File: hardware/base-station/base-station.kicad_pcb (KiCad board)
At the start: 4 copper layers, 30.3 x 90.5 mm, 114 parts, among them J2 USB4110GFA, J4 S3B-XH-A, J6 Conn_01x04, Q1 FS8205A, Q2 FS8205A, Q3 FS8205A, U1 W25Q128JVSIQ, U12 MP2672AGD-0000-Z, U14 DW01A, U15 479480001, U2 TPS61023DRLR, U22 TPS22918DBVR, U3 ESP32-S3RH2, U5 BQ21040DBVR, U9 TPS63020DSJR, Y1 SC-32S-32.768kHz-12.5pF, Y2 ECS-400-10-37B2-CKY-TR

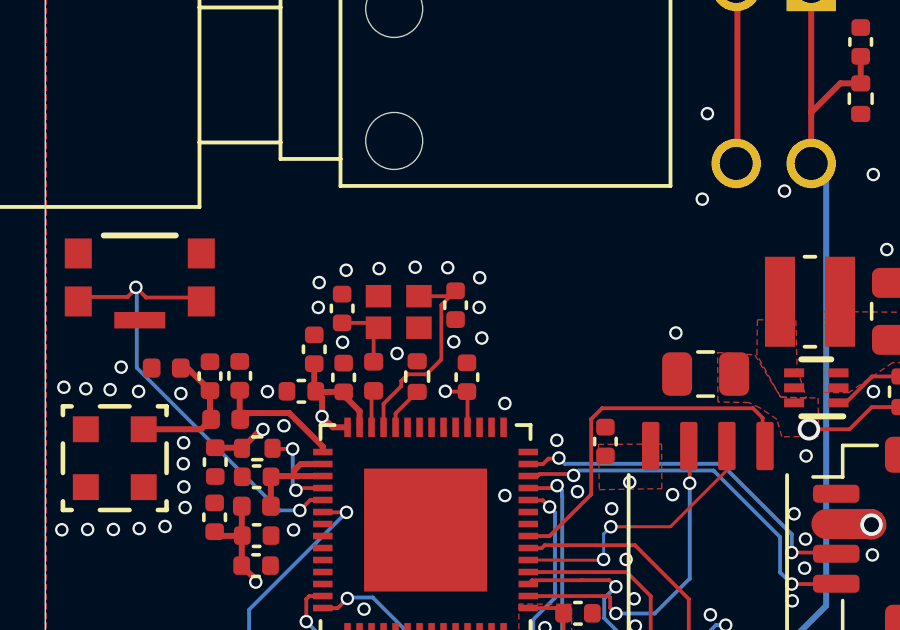
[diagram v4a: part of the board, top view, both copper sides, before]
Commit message: hardware: drop the 24 nH series inductor from all three S3 crystal legs
Every ESP32-S3 board put a 24 nH in series with XTAL_P -- base L2, rocket L3,
LoRa L10 -- inherited from a reference design. The P4's crystal never had one.
Measured against what it actually does at 40 MHz, it does not earn the part:

  reactance         6.0 ohm, against 331 ohm for the 12 pF load cap
  frequency effect  -1.1 ppm (it makes the leg's cap look 1.8% larger)
  low-pass corner   297 MHz with the load cap -- trims the 8th harmonic up,
                    which was its only defensible function
  resonance w/ C0   726 MHz, where the oscillator has no gain, so it was
                    never a risk either

Removing it leaves each XTAL_P as a direct U.54 - Y.3 - C.1 connection and
takes one 0402 plus one BOM line out of all three boards. The RF matching
networks are untouched: rocket keeps L1 4.3 nH / L2 2.7 nH / L4 2 nH, base
keeps L4 4.3 nH / L7 2.7 nH / L3 2 nH, LoRa keeps L11 2 nH (supply filter --
that board has no antenna and LNA_IN is deliberately unconnected).

Frequency error at 12 pF after the change:

  lora   Y6 -> U28   11.97 mm avg   +8.6 ppm
  rocket Y2 -> U15   11.54 mm avg   +9.2 ppm
  rocket Y4 -> U17   11.97 mm avg   +8.6 ppm
  base   Y2 -> U3     7.58 mm avg  +15.1 ppm   <- #704 still open

Cross-board BOM: the 24 nH line (LQW15AN24NH00D) is retired, quantities
cleared rather than the row deleted, per the sheet's existing convention.
System cost 122.58 -> 122.28 per set. All four costed boards still reconcile
exactly: 424 fitted parts, 0 quantity mismatches, 0 parts without a BOM row.

Refs #704

Co-Authored-By: Claude Opus 5 <noreply@anthropic.com>
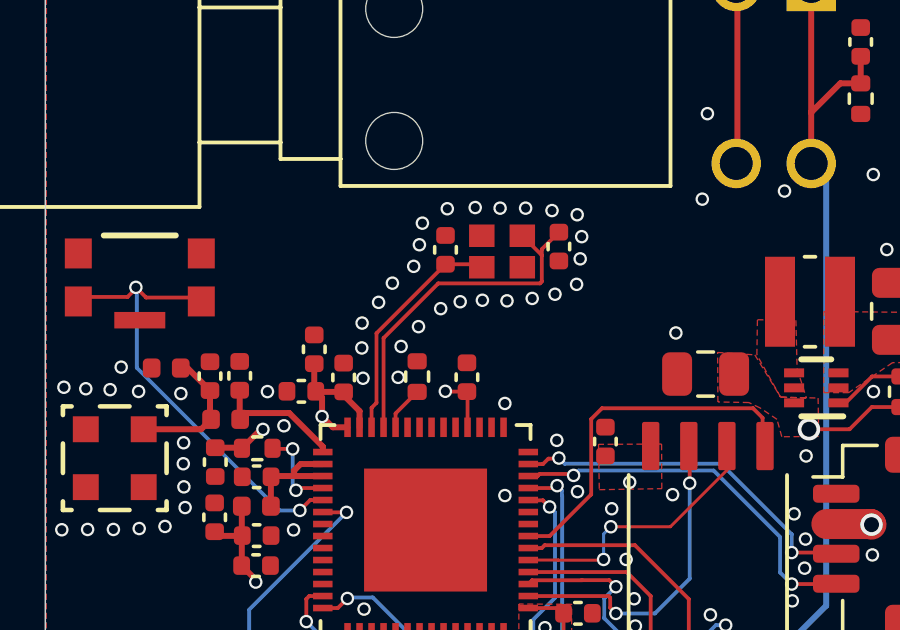
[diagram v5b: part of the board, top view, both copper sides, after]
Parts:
- removed L2: 24 nH, Inductor_SMD:L_0402_1005Metric
- C3, C6: value 18 pF -> 12 pF
- Y1: value SC-32S-32.768kHz-12.5pF -> ABS07-32.768KHZ-T
- moved Y2 3.99 mm to (62.6, 142.5)
- moved C3 3.96 mm to (60.7, 142.5)
- moved C6 3.96 mm to (64.5, 142.4)
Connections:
- C23 pad 1: Net-(U22-QOD) -> V_SWITCH
- C3 pad 1: Net-(C3-Pad1) -> Net-(U3-XTAL_P)
- C34 pad 1: VCC -> V_SWITCH
- C59 pad 1: Net-(U22-QOD) -> V_SWITCH
- C8 pad 1: +3V3 -> Net-(U3-CHIP_PU)
- L8 pad 1: VCC -> V_SWITCH
- R1 pad 1: Net-(U3-CHIP_PU) -> +3V3
- R1 pad 2: +3V3 -> Net-(U3-CHIP_PU)
- U2 pad 2: VCC -> V_SWITCH
- U2 pad 3: VCC -> V_SWITCH
- U22 pad 5: Net-(U22-QOD) -> V_SWITCH
- U22 pad 6: Net-(U22-QOD) -> V_SWITCH
- U9 pad 10: Net-(U22-QOD) -> V_SWITCH
- U9 pad 11: Net-(U22-QOD) -> V_SWITCH
- Y2 pad 3: Net-(C3-Pad1) -> Net-(U3-XTAL_P)
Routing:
- net Net-(U3-XTAL_P): track 1.24 -> 7.71 mm
- net Net-(U3-XTAL_N): track 7.20 -> 11.8 mm
- net Net-(C3-Pad1): track 2.48 -> 0.00 mm
- net Net-(U3-CHIP_PU): track 3.03 -> 4.89 mm
- net +3V3: track 18.9 -> 17.1 mm
- net GND: track 2.69 -> 2.70 mm, vias 124 -> 138
- added copper zone on F.Cu, net V_SWITCH
- removed copper zone on F.Cu, net Net-(U22-QOD)

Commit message: hardware(base-station): lengthen the 40 MHz clock legs to match the other boards
#704: the base station's crystal traces were less than half the length of the
other three networks, so the 12 pF load caps that suit every other board left
this one under-loaded and running fast. Y2 moved further from U3 and both legs
re-routed; XTAL_P 6.76 -> 8.94 mm, XTAL_N 8.41 -> 11.83 mm, average 7.58 ->
10.38 mm.

All four networks are now matched to within 2.3 ppm:

  lora   Y6 -> U28   11.97 mm avg   +8.6 ppm
  rocket Y2 -> U15   11.54 mm avg   +9.2 ppm
  rocket Y4 -> U17   11.97 mm avg   +8.6 ppm
  base   Y2 -> U3    10.38 mm avg  +10.9 ppm

Every clock net is on a single layer with zero vias, per Espressif's rule.

Stopping at +10.9 rather than chasing the last 0.9 ppm of copper is deliberate.
The absolute figure assumes C_m = 5 fF and C_0 = 2 pF -- typical for a 3225
AT-cut but NOT read off the ECS datasheet -- and sweeping those across
plausible values puts this network anywhere from +8.1 to +15.4 ppm, so 0.9 ppm
is well inside the model's own uncertainty. What the model does resolve
reliably is the difference between boards, since that depends only on delta
C_L, and by that measure the four are now equivalent.

DEFERRED, unchanged from the issue: measure the 40 MHz output on the first
article and trim if needed. The trim needs no layout work -- C3/C6 at 13 pF
moves this network to +1.8 ppm in the same footprint.

Refs #704

Co-Authored-By: Claude Opus 5 <noreply@anthropic.com>
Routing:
- net Net-(U3-XTAL_P): track 7.71 -> 8.94 mm
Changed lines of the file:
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@@
 	)
 	(via
-		(at 58.51 144.23)
+		(at 57.97 143.92)
 		(size 0.45)
 		(drill 0.3)
@@
 	)
 	(via
-		(at 59.68 143.03)
+		(at 58.49 142.52)
 		(size 0.45)
 		(drill 0.3)
@@
 	)
 	(via
-		(at 60.58 144.44)
+		(at 60.46 144.57)
 		(size 0.45)
 		(drill 0.3)
@@
 	)
 	(via
-		(at 59.87 142.31)
+		(at 59.29 142.14)
 		(size 0.45)
 		(drill 0.3)
@@
 	)
 	(via
-		(at 58.97 143.59)
+		(at 58.04 143.2)
 		(size 0.45)
 		(drill 0.3)
@@
 	)
 	(segment
-		(start 58.44 145.26)
-		(end 60.74 142.96)
+		(start 61.85 142.96)
+		(end 61.95 143.06)
 		(width 0.127)
 		(layer "F.Cu")
@@
 	)
 	(segment
-		(start 61.85 142.96)
-		(end 61.95 143.06)
+		(start 58.44 143.16)
+		(end 58.64 142.96)
 		(width 0.127)
 		(layer "F.Cu")
@@
 	)
 	(segment
-		(start 58.275 148.395)
-		(end 58.275 147.745)
+		(start 58.275 147.745)
+		(end 58.44 147.58)
 		(width 0.127)
 		(layer "F.Cu")
@@
 	)
 	(segment
-		(start 58.44 147.58)
-		(end 58.44 145.26)
+		(start 60.74 142.96)
+		(end 61.85 142.96)
 		(width 0.127)
 		(layer "F.Cu")
@@
 	)
 	(segment
-		(start 60.74 142.96)
-		(end 61.85 142.96)
+		(start 58.64 142.96)
+		(end 60.74 142.96)
 		(width 0.127)
 		(layer "F.Cu")
@@
 	)
 	(segment
-		(start 58.275 147.745)
-		(end 58.44 147.58)
+		(start 58.44 147.58)
+		(end 58.44 143.16)
+		(width 0.127)
+		(layer "F.Cu")
+		(net "Net-(U3-XTAL_P)")
+	)
+	(segment
+		(start 58.275 148.395)
+		(end 58.275 147.745)
 		(width 0.127)
 		(layer "F.Cu")

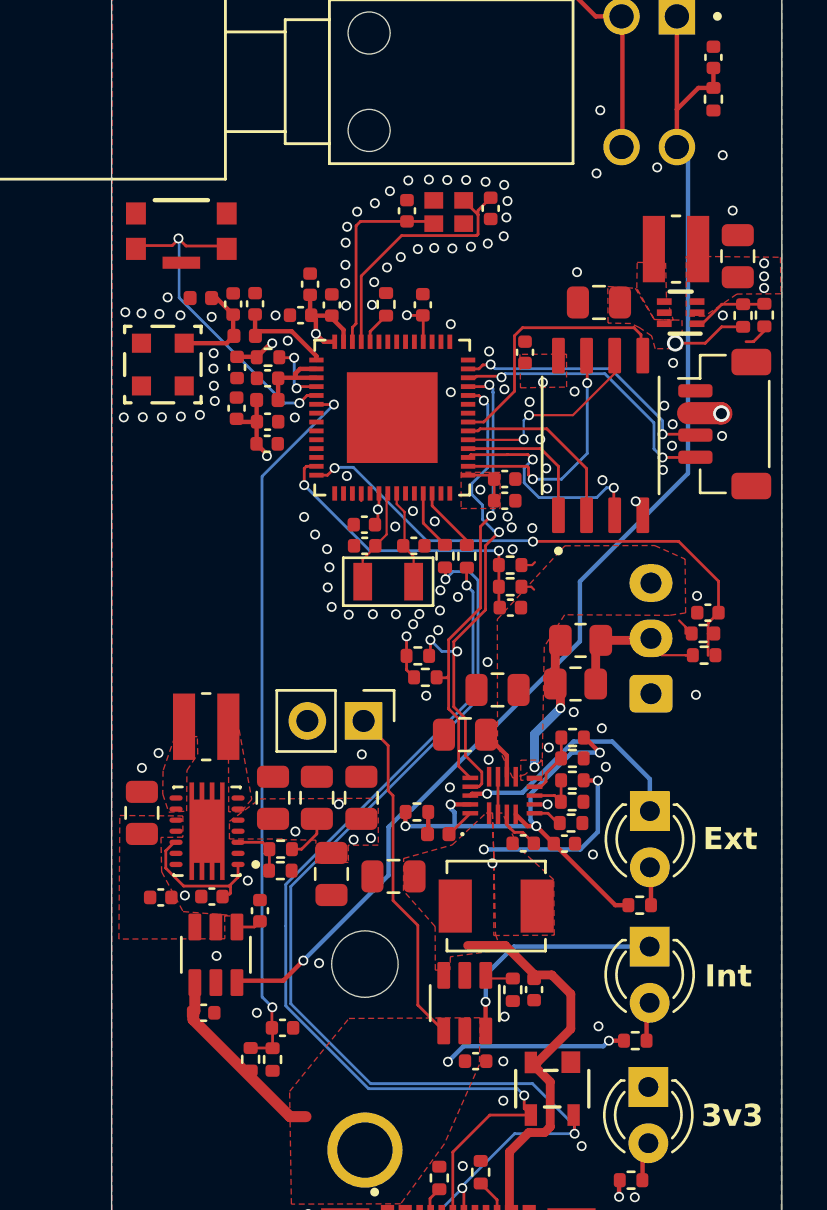
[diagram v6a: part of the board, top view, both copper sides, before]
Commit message: hardware(base-station): pre-fab fixes -- JLC stackup, RF feed, R17/R18, EN margin
The board changes the 2026-08-02 pre-manufacturing review called for. Board is
DRC-clean: 0 errors, 0 unconnected items, 0 schematic-parity issues.

Electrical:
- R17 10 k -> 18.7 k and R18 1 k, both with MPNs that match their values. Both
  previously carried RC0402FR-075K11L (5.11 k). Built to that MPN the TPS61023
  EN pin would sit at 1.65 V driven low, above the 1.2 V V_EN_H ceiling, and the
  LoRa power-cycle recovery would never work with no symptom. 18.7 k/1 k gives
  0.174 V against the 0.35 V guaranteed-low floor, and is already a fleet MPN so
  it adds no BOM line.
- Antenna matching reduced to Molex section 6.0: L4 4.3 nH shunt alone, with
  C2 = 0 ohm realised as a direct trace. C25/C26/L7 removed. The previous
  four-element network put 4.3 nH in parallel with 1.5 pF, which is -j127.8 ohm
  at 2.44 GHz where the Molex reference is +j65.9 ohm -- a sign inversion, not a
  value shift. Accepted trade: this build has no tuning provision, so it must be
  characterised with the cell installed and the result carried into the next
  revision.
- U15 fixing pads 1-3 left individually unconnected. AS-479480001 calls them
  fixing pads and never specifies their net; grounding them is an unforced risk
  on an LDS part whose plating wraps the body.

Stackup and rules, now JLCPCB standard 4-layer:
- JLC04161H-7628: 0.2104 mm 7628 prepreg (Er 4.4), 0.5 oz inner copper, 1.065 mm
  core, ENIG, 1.5862 mm. The previous 0.1 mm prepreg and 1 oz inner layers were
  not a stackup any standard 4-layer order builds.
- RF feed re-solved for the new dielectric: 0.20 -> 0.36 mm, giving 49.7 ohm as
  CPWG at the 0.15 mm pour gap. At 0.20 mm on the new stackup it would have been
  ~68 ohm. New RF netclass carries the width and clearance.
- min_clearance 0.09 -> 0.10 (0.09 falls in the JLC 3.0-3.5 mil upcharge band),
  min_via_diameter 0.40 -> 0.45, annular 0.05 -> 0.075, drill 0.1 -> 0.3, silk
  text 0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
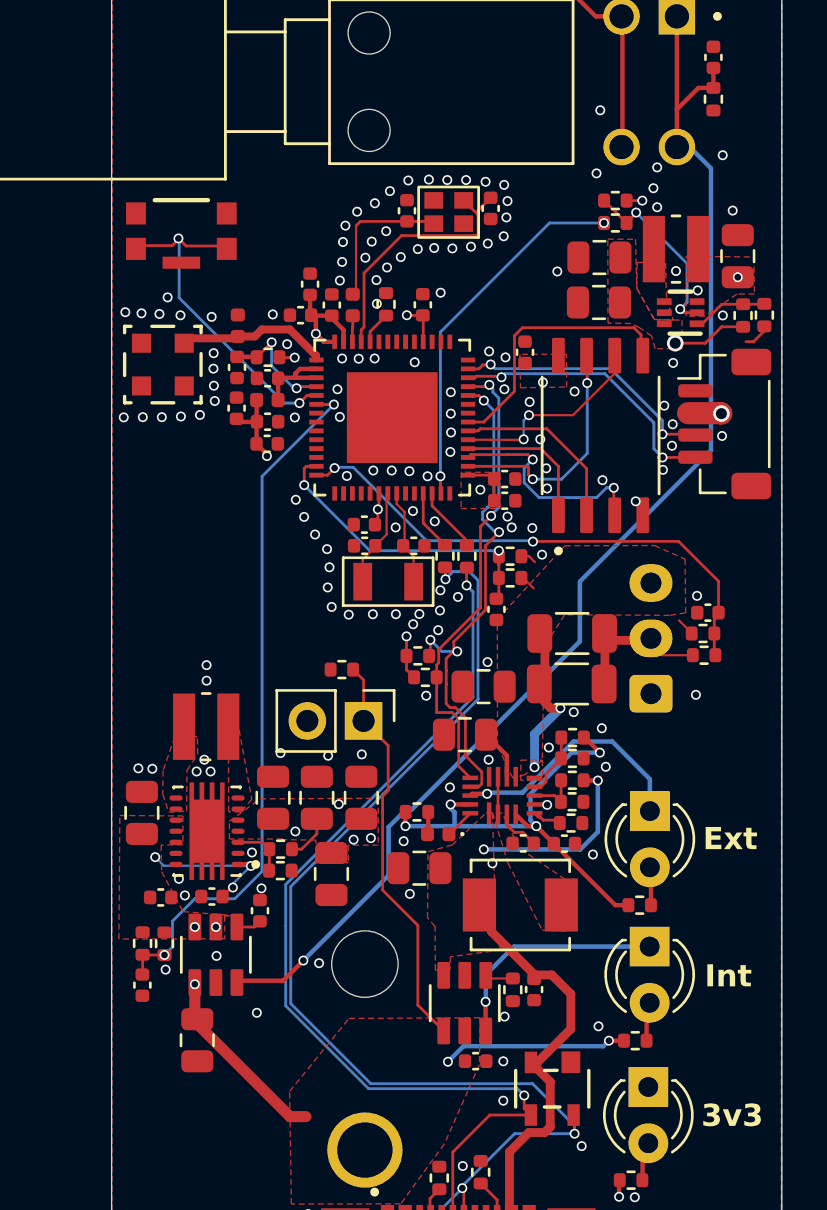
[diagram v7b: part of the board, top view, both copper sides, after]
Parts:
- removed C25, C26: 1.5 pF, Capacitor_SMD:C_0402_1005Metric
- removed L7: 2.7 nH, Inductor_SMD:L_0402_1005Metric
- added C41: 22 uF, Capacitor_SMD:C_0805_2012Metric, F.Cu at (69.4, 144.6)
- added L2: 24 nH, Inductor_SMD:L_0402_1005Metric, F.Cu at (58.3, 146.7)
- added R17: 18.7 k, Resistor_SMD:R_0402_1005Metric, F.Cu at (70.2, 142.0)
- added R18: 1 k, Resistor_SMD:R_0402_1005Metric, F.Cu at (70.2, 143.0)
- added R53: 210 k, Resistor_SMD:R_0402_1005Metric, F.Cu at (57.8, 163.2)
- C42: value 1 uF -> 22 uF; footprint Capacitor_SMD:C_0402_1005Metric -> Capacitor_SMD:C_0805_2012Metric
- R43: value 6.04 k -> 10 k
- R45, R47: footprint Resistor_SMD:R_0805_2012Metric -> Resistor_SMD:R_1206_3216Metric
- moved R46 7.87 mm to (48.8, 175.6), turned to 90 degrees
- moved C30 6.62 mm to (48.8, 177.4), turned to -90 degrees
- moved R44 6.51 mm to (49.8, 175.6), turned to -90 degrees
- moved L4 2.09 mm to (53.1, 147.7), turned to -90 degrees
- moved C42 1.27 mm to (51.3, 179.9), turned to -90 degrees
- moved C48 1.23 mm to (61.3, 172.2)
- moved L6 1.09 mm to (65.9, 173.8)
- moved C54 0.65 mm to (64.2, 164.0)
- moved C55 0.64 mm to (64.8, 160.5), turned to 90 degrees
- moved R47 0.49 mm to (68.2, 161.6)
- moved R40 0.40 mm to (65.4, 159.1)
- moved R42 0.40 mm to (65.4, 158.1)
- moved R45 0.17 mm to (68.2, 163.8)
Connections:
- C29 pad 1: Net-(U9-EN) -> V_SWITCH
- C3 pad 1: Net-(U3-XTAL_P) -> Net-(C3-Pad1)
- R44 pad 1: VCC -> V_SWITCH
- U2 pad 2: V_SWITCH -> Net-(U2-EN)
- U3 pad 1: Net-(U3-LNA_IN) -> Net-(U15-Feed)
- U3 pad 10: M_MOSI -> unconnected-(U3-GPIO5-Pad10)
- U3 pad 11: M_FLASH_CS -> unconnected-(U3-GPIO6-Pad11)
- U3 pad 12: M_MISO -> unconnected-(U3-GPIO7-Pad12)
- U3 pad 27: unconnected-(U3-GPIO21-Pad27) -> LoRa_EN
- U3 pad 9: M_SCK -> unconnected-(U3-GPIO4-Pad9)
- U9 pad 1: Net-(U9-EN) -> V_SWITCH
- U9 pad 12: Net-(U9-EN) -> V_SWITCH
- Y2 pad 3: Net-(U3-XTAL_P) -> Net-(C3-Pad1)
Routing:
- net V_SWITCH: track 0.00 -> 54.2 mm, vias 0 -> 7
- net LoRa_EN: track 0.00 -> 16.7 mm, vias 0 -> 2
- net VCC: track 112.5 -> 99.3 mm, vias 5 -> 3
- net Net-(U2-EN): track 0.00 -> 8.35 mm, vias 0 -> 2
- net Net-(U3-XTAL_P): track 8.94 -> 1.18 mm
- net Net-(C3-Pad1): track 0.00 -> 6.79 mm
- net Net-(U9-EN): track 6.55 -> 0.00 mm
- net Net-(U3-LNA_IN): track 4.46 -> 0.00 mm
- net Net-(U5-TS): track 15.5 -> 18.2 mm
- net Net-(U15-Feed): track 4.64 -> 6.83 mm
- net +3V3: track 17.1 -> 18.6 mm, vias 11 -> 12
- net Net-(U22-ON): track 57.1 -> 58.0 mm
- net Net-(U12-MID): track 6.41 -> 7.08 mm
- net Volt_Read: track 32.4 -> 31.8 mm
- net VBUS: track 33.2 -> 33.8 mm
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
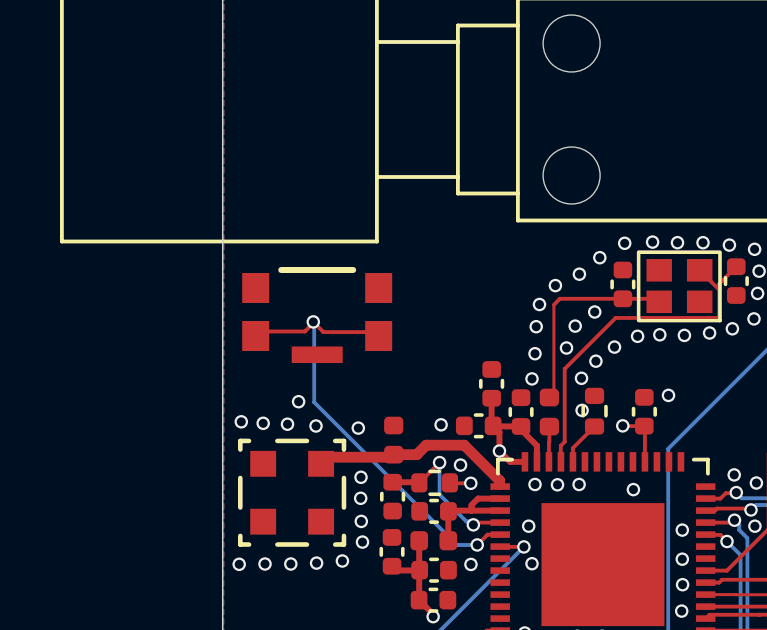
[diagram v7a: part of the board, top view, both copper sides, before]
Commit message: hardware(rocket-computer): V9 pre-fab review close-out -- every finding fixed, measured, or waived
Closes the 2026-08-04..09 pre-manufacturing review (170 raw findings).
WORKLIST.md is the closing record: D-1..D-4 decided, H-1..H-10 and
M-1..M-25 dispositioned, Lows annotated, bench list is the remainder.

Power architecture:
- All four peripheral branches converted low-side N-FET -> integrated
  high-side switches (U26/U28 TPS22811LRPWR, U27/U29 TPS22810DRVR);
  U30 TPS22810DRVR gates the P4 domain. Every connector ground is now
  hard GND; the 12 EXP lines stay resistor-free by design (H-3/D-4).
  J3 and J4 power pins swapped ends -- fab notes B6/B7 carry the
  harness warnings.
- Q11 (CSD25404Q3) reverse-polarity P-FET at the battery input on a
  new TI-pattern footprint; CR2 re-purposed as connector ESD clamp
  upstream of it (M-9/M-10). Kelvin sense at R72 preserved.
- P4 rail self-latch: D9 (BAV170M) OR-gates S3 request with P4 hold,
  C105 rides the P4 through its own reset (H-4; firmware in #718).
- eFuse UVLO deglitch C94 (H-1); brownout decided as clean-reboot,
  ECO hold-up claims corrected in power-eco.md (H-8/D-3).
- Pyro gate-drive stiffened: R22 -> 5.11k, R78-R81 shunts (H-2).
- Servo budget decided at 3 A set by the In2 stretch; ILIM left open
  at 11.6 A; SERVO_IMON flight data gates any increase (D-1).

Component and BOM:
- TPS2121 ILIM 18.7k -> 49.9k (real protection at 2.26 A typ, M-5).
- IMON scaling: R85 -> 2.2k (3 A camera), R88 -> 1k (servo open).
- C27 VDD_SPI 10u -> 1u per HDG (M-4); switch VIN bypass 100n -> 1u;
  C40/C76 consolidation; C65 MPN fixed (was a 390 pF part number
  under a 100 nF value -- would have misassembled the buck bypass).
- SW2/SW3 on the R-667995 tact switch, footprint imported and pads
  renumbered to match; FB-network DNP parts carry MPNs for the v3.x
  flip (M-22); bom.csv regenerated: 79 lines / 243 placements, every
  part carries an MPN. Priced BOMs evicted from board dirs (they live
  in Documents/Circuit Board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
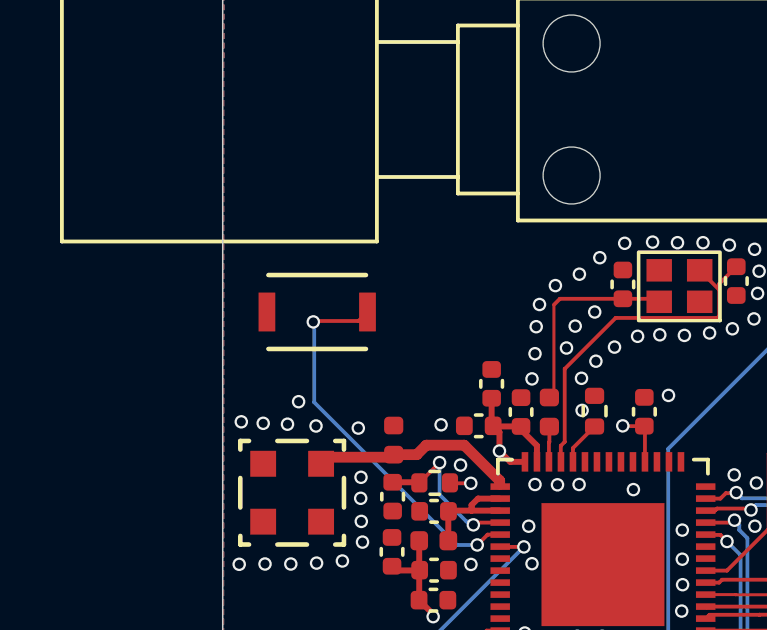
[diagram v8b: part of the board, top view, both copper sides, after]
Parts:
- S3: value KMR221GLFS -> R-667995; footprint Footprints:SW_KMR221GLFS -> Footprints:R-667995_MIT
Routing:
- net Net-(U3-GPIO0): track 15.5 -> 13.0 mm
